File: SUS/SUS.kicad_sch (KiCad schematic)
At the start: 64 parts, among them J1 ESP32_Connector_0, J2 ESP32_Connector_1, J3 I2C, J4 I2C, J5 I2C, J6 ADC, J7 WS, U1 TJA1051T, U2 ADS8320EB_250, U3 ICM-42688-P, U4 S1001-46R, U5 S1001-46R, U6 S1001-46R

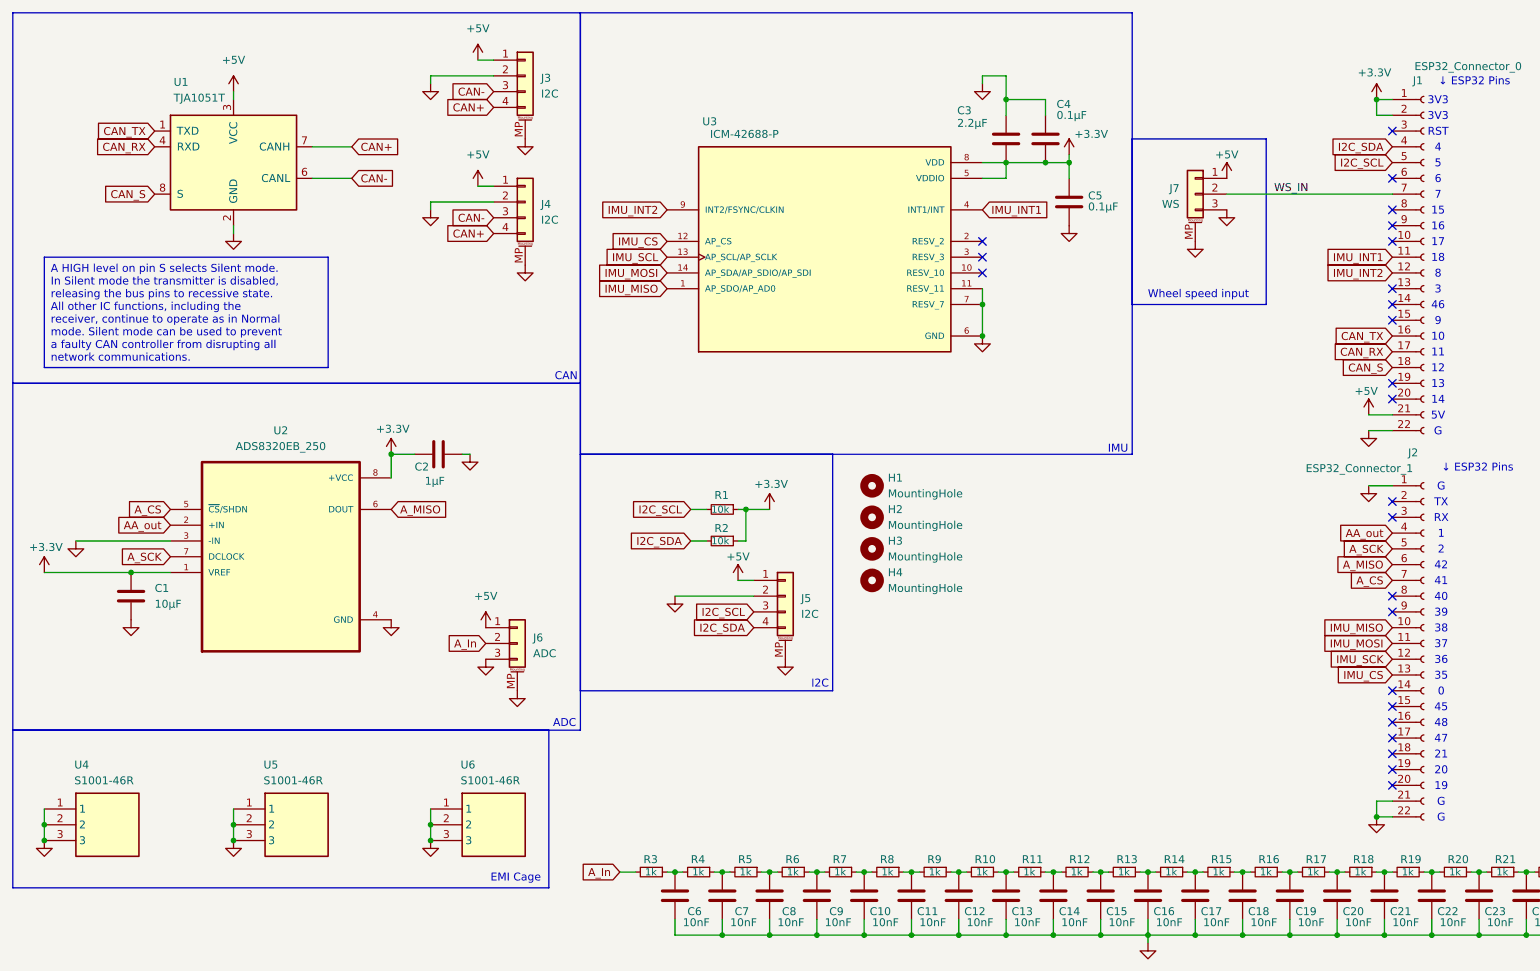
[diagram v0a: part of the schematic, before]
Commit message: added pads to connect 3.3v or 5v to lin pots & other last minute changes
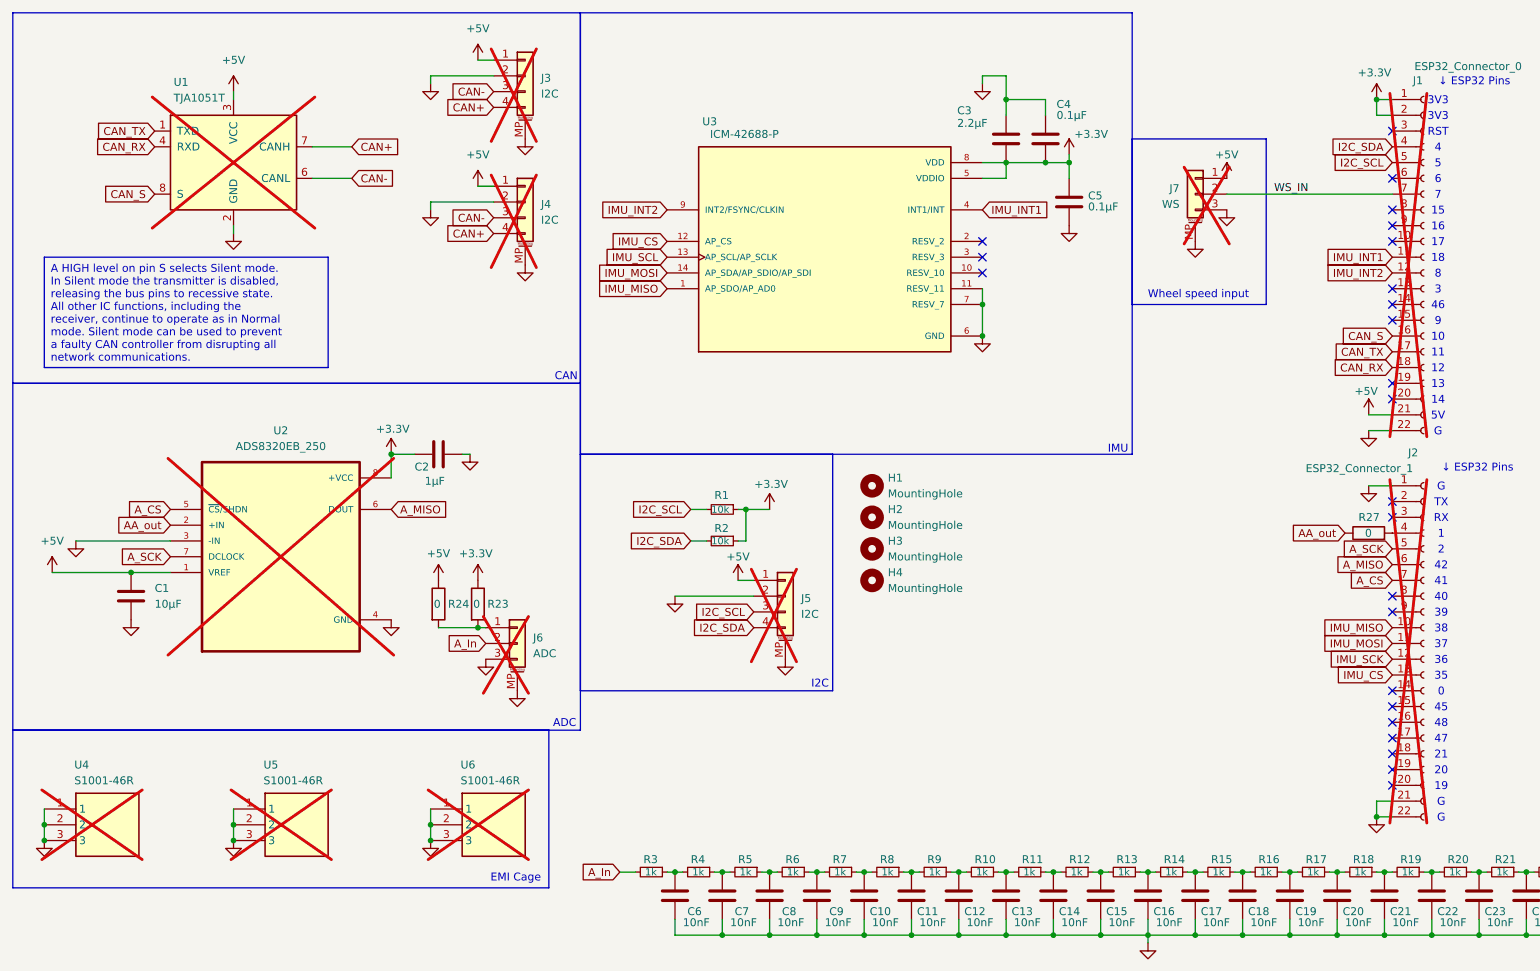
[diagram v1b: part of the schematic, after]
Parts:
- added R23, R24, R27: 0, Resistor_SMD:R_0402_1005Metric_Pad0.72x0.64mm_HandSolder, symbol Device:R
- J1, J2, J3, J4, J5, J6, J7, U1, U2, U4, U5, U6: now not fitted
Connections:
- net +3.3V: now also R23.1; no longer C1.1, U2.1 (VREF)
- net +5V: now also C1.1, U2.1 (VREF), R24.1; no longer J6.1 (Pin_1)
- net AA_out: now also R27.1; no longer J2.4 (Pin_4)
- net CAN_RX: now also J1.18 (Pin_18); no longer J1.17 (Pin_17)
- net CAN_S: now also J1.16 (Pin_16); no longer J1.18 (Pin_18)
- net CAN_TX: now also J1.17 (Pin_17); no longer J1.16 (Pin_16)
- new net: J6.1 (Pin_1), R23.2, R24.2
- new net: J2.4 (Pin_4), R27.2

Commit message: Removed Vias
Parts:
- U3: footprint ICM-42688-P:PQFN50P300X250X97-14N -> IMU:ICM-42688-P
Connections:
- net IMU_SCL is gone; now on net IMU_SCK: U3.13 (AP_SCL/AP_SCLK)
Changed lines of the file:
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@@
 		)
 	)
-	(global_label "IMU_SCL"
+	(global_label "IMU_SCK"
 		(shape input)
 		(at 118.11 52.07 180)
@@
 		)
 		(property "Intersheetrefs" "${INTERSHEET_REFS}"
-			(at 107.2629 52.07 0)
+			(at 107.021 52.07 0)
 			(effects
 				(font
@@
 			)
 		)
-		(property "Footprint" "ICM-42688-P:PQFN50P300X250X97-14N"
+		(property "Footprint" "IMU:ICM-42688-P"
 			(at 143.51 49.53 0)
 			(effects

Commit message: Complete re-design. Readme still needs to be updated.
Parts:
- removed H1, H2, H3, H4: MountingHole, MountingHole:MountingHole_2.7mm_M2.5, symbol Mechanical:MountingHole
- removed J3, J4, J5: I2C, Connector_Hirose:Hirose_DF3EA-04P-2H_1x04-1MP_P2.00mm_Horizontal, symbol Connector_Generic_MountingPin:Conn_01x04_MountingPin
- removed J6: ADC, Connector_Hirose:Hirose_DF3EA-03P-2H_1x03-1MP_P2.00mm_Horizontal, symbol Connector_Generic_MountingPin:Conn_01x03_MountingPin
- removed J7: WS, Connector_Hirose:Hirose_DF3EA-03P-2H_1x03-1MP_P2.00mm_Horizontal, symbol Connector_Generic_MountingPin:Conn_01x03_MountingPin
- removed R23, R24, R27: 0, Resistor_SMD:R_0402_1005Metric_Pad0.72x0.64mm_HandSolder, symbol Device:R
- removed U1: TJA1051T, Package_SO:SOIC-8_3.9x4.9mm_P1.27mm, symbol Interface_CAN_LIN:TJA1051T
- removed U2: ADS8320EB_250, ADS8320EB_250:DGK0008A_L, symbol ADS8320EB:ADS8320EB_250
- removed U3: ICM-42688-P, IMU:ICM-42688-P, symbol ICM-42688-P:ICM-42688-P
- removed U4, U5, U6: S1001-46R, S1001-46R:S100146R, symbol S1001-46R:S1001-46R
- added C26: 0.33μF, Capacitor_SMD:C_0603_1608Metric, symbol Device:C
- added C27: 0.1μF, Capacitor_SMD:C_0603_1608Metric, symbol Device:C
- added C28: 0.1μF, Capacitor_SMD:C_0402_1005Metric_Pad0.74x0.62mm_HandSolder, symbol Device:C
- added H1, H2, H3, H4: MountingHole_Pad, MountingHole:MountingHole_2.2mm_M2_Pad_TopOnly, symbol Mechanical:MountingHole_Pad
- added J3: D25P13A4GV00LF, D25:CONN_D25P_AMP, symbol D25:D25P13A4GV00LF
- added JP1: SolderJumper_2_Open, Jumper:SolderJumper-2_P1.3mm_Open_TrianglePad1.0x1.5mm, symbol Jumper:SolderJumper_2_Open
- added R23, R24, R25: 10k, Capacitor_SMD:C_0201_0603Metric, symbol Device:R_Small
- added U1: L7805, Package_TO_SOT_THT:TO-220F-3_Vertical, symbol Regulator_Linear:L7805
- added U2: ADS1015IDGSR, ADC:SOP50P490X110-10N, symbol ADC:ADS1015IDGSR
- added U3: ICM-42688-P, IMU:PQFN50P300X250X97-14N, symbol IMU:ICM-42688-P
- added U4: TJA1051TK-3, Package_DFN_QFN:DFN-8-1EP_3x3mm_P0.65mm_EP1.55x2.4mm, symbol Interface_CAN_LIN:TJA1051TK-3
- C1: value 10μF -> 0.1μF; footprint Capacitor_SMD:C_0402_1005Metric_Pad0.74x0.62mm_HandSolder -> Capacitor_SMD:C_0201_0603Metric
- C10, C11, C12, C13, C14, C15, C16, C17, C18, C19, C20, C21, C22, C23, C24, C25, C6, C7, C8, C9: LCSC PN C76941 -> (none)
- C2: value 1μF -> 0.1μF
- J1, J2: now fitted
- R10, R11, R12, R13, R14, R15, R16, R17, R18, R19, R20, R21, R22, R3, R4, R5, R6, R7, R8, R9: JLCpart# (none) -> C2906988; LCSC PN C270365 -> (none)
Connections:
- net WS_IN is gone; now on net CAN_RX: J1.7 (Pin_7)
- net +3.3V: now also C28.1, U3.5 (VDDIO), U3.8 (VDD), U4.5 (VIO); no longer C2.1
- net +5V: now also C2.1, C27.2, J3.16, J3.20, J3.9, U1.3 (OUT), U4.3 (VCC); no longer C1.1
- net AA_out: now also JP1.1 (A), U2.4 (AIN0)
- net A_CS: now also J2.9 (Pin_9), R25.2, U2.2 (ALERT/RDY); no longer J2.7 (Pin_7)
- net A_In: now also J3.15
- net CAN+: now also J3.10, J3.22, U4.7 (CANH)
- net CAN-: now also J3.11, J3.23, U4.6 (CANL)
- net CAN_RX: now also U4.4 (RXD); no longer J1.18 (Pin_18)
- net CAN_S: now also U4.8 (S); no longer J1.16 (Pin_16)
- net CAN_TX: now also J1.6 (Pin_6), U4.1 (TXD); no longer J1.17 (Pin_17)
- net GND: now also C26.1, C27.1, C28.2, H1.1, H2.1, H3.1, H4.1, J3.14, J3.17, J3.4, U1.2 (GND), U2.1 (ADDR), U2.3 (GND), U2.5 (AIN1), U3.11 (RESV_11), U3.6 (GND), U3.7 (RESV_7), U4.2 (GND), U4.9 (GND)
- net I2C_SCL: now also J1.4 (Pin_4), J3.19; no longer J1.5 (Pin_5)
- net I2C_SDA: now also J1.5 (Pin_5), J3.18; no longer J1.4 (Pin_4)
- net IMU_CS: now also J1.16 (Pin_16), U3.12 (AP_CS); no longer J2.13 (Pin_13)
- net IMU_INT1: now also U3.4 (INT1/INT)
- net IMU_INT2: now also U3.9 (INT2/FSYNC/CLKIN)
- net IMU_MISO: now also J1.19 (Pin_19), U3.1 (AP_SDO/AP_AD0); no longer J2.10 (Pin_10)
- net IMU_MOSI: now also J1.17 (Pin_17), U3.14 (AP_SDA/AP_SDIO/AP_SDI); no longer J2.11 (Pin_11)
- net ESP_ADC: now reaches J1.20 (Pin_20)
- net ESP_ADC: now also JP1.2 (B)
- net GPIO 20: now reaches J2.19 (Pin_19)
- net GPIO 20: now also J3.2
- net TX: now reaches J2.2 (Pin_2)
- net TX: now also J3.13
- net GPIO 19: now reaches J2.20 (Pin_20)
- net GPIO 19: now also J3.3
- net RX: now reaches J2.3 (Pin_3)
- net RX: now also J3.12
- net A_SDA: now reaches J2.8 (Pin_8)
- net A_SDA: now also R24.2, U2.9 (SDA)
- net A_MISO: no longer names the net of J2.6 (Pin_6)
- net A_SCK: no longer names the net of J2.5 (Pin_5)
- net IMU_SCK renamed GPIO 36
- net GPIO 36: now also J3.6
- new net +12V: C26.2, J3.1, U1.1 (IN)
- new net 3.3V: R23.1, R24.1, R25.1
- new net 5V: C1.1, U2.8 (VDD)
- new net A_SCL: J2.7 (Pin_7), R23.2, U2.10 (SCL)
- new net GPIO 35: J2.13 (Pin_13), J3.5
- new net GPIO 37: J2.11 (Pin_11), J3.7
- new net GPIO 38: J2.10 (Pin_10), J3.8
- new net IMU_SCL: J1.18 (Pin_18), U3.13 (AP_SCL/AP_SCLK)
- no-connect marks 24 -> 20
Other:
- note added: "3.3v pullup or 5v????"
- note removed: "EMI Cage"
- note removed: "Wheel speed input"
- moved on the sheet: R1, R2

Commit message: Changed CAN transceiver.
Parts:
- removed C28: 0.1μF, Capacitor_SMD:C_0402_1005Metric_Pad0.74x0.62mm_HandSolder, symbol Device:C
- removed H4: MountingHole_Pad, MountingHole:MountingHole_2.2mm_M2_Pad_TopOnly, symbol Mechanical:MountingHole_Pad
- removed U1: L7805, Package_TO_SOT_THT:TO-220F-3_Vertical, symbol Regulator_Linear:L7805
- removed U4: TJA1051TK-3, Package_DFN_QFN:DFN-8-1EP_3x3mm_P0.65mm_EP1.55x2.4mm, symbol Interface_CAN_LIN:TJA1051TK-3
- added U1: HT7333, HT7333:IC_HT7333, symbol HT7333:HT7333
- added U5: SN65HVD232, Package_SO:SOIC-8_3.9x4.9mm_P1.27mm, symbol Interface_CAN_LIN:SN65HVD232
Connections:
- net 3.3V is gone; now on net +3.3V: R23.1, R24.1, R25.1
- net +12V: now also U1.2 (VIN)
- net +3.3V: now also C2.1, U5.3 (VCC)
- net +5V: now also U1.3 (VOUT); no longer C2.1
- net CAN+: now also J3.11, J3.23, U5.7 (CANH); no longer J3.10, J3.22
- net CAN-: now also J3.10, J3.22, U5.6 (CANL); no longer J3.11, J3.23
- net CAN_RX: now also J2.6 (Pin_6), U5.4 (R); no longer J1.7 (Pin_7)
- net CAN_TX: now also J2.5 (Pin_5), U5.1 (D); no longer J1.6 (Pin_6)
- net GND: now also U1.1 (GND), U5.2 (GND); no longer U2.5 (AIN1)
- net I2C_SCL: now also J2.16 (Pin_16); no longer J1.4 (Pin_4)
- net I2C_SDA: now also J2.17 (Pin_17); no longer J1.5 (Pin_5)
- no-connect marks 20 -> 17

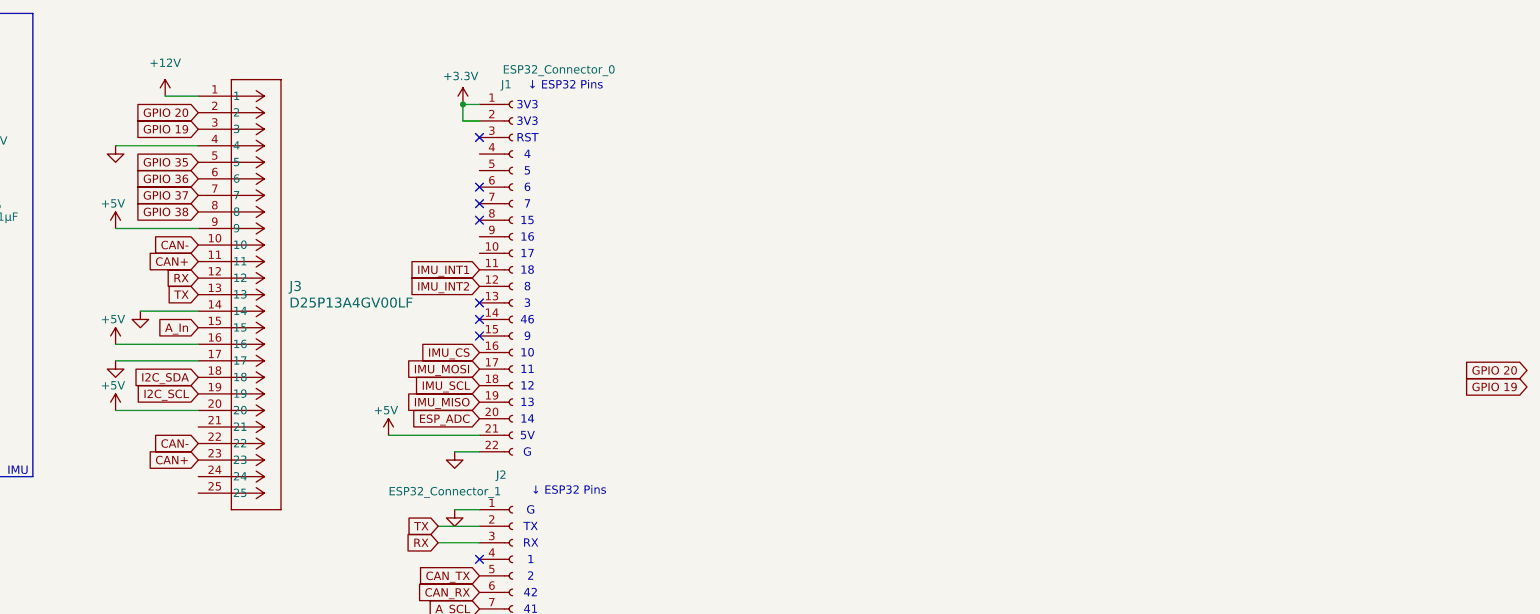
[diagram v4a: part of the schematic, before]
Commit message: Fixed DRC errors
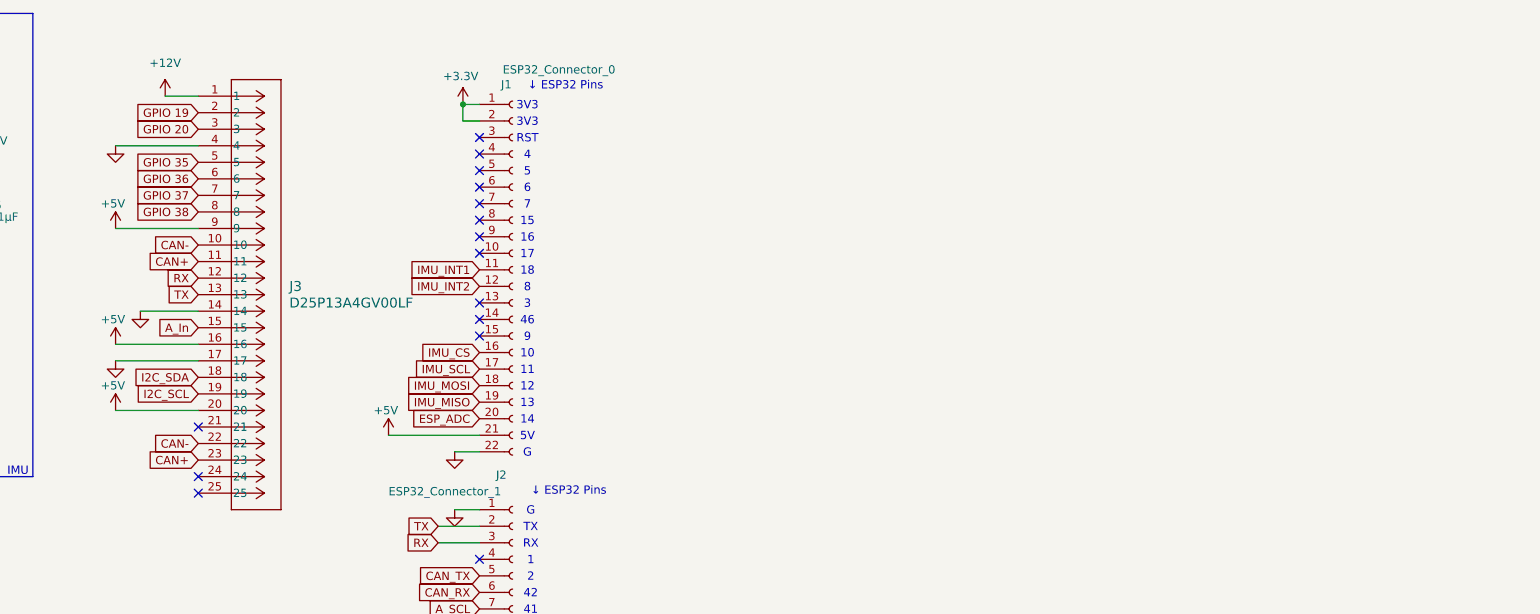
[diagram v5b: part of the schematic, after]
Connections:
- net GPIO 19: now also J3.2; no longer J3.3
- net GPIO 20: now also J3.3; no longer J3.2
- net IMU_MOSI: now also J1.18 (Pin_18); no longer J1.17 (Pin_17)
- net IMU_SCL: now also J1.17 (Pin_17); no longer J1.18 (Pin_18)
- no-connect marks 17 -> 24

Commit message: Minor Changes
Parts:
- U1: value HT7333 -> HT7350-A
- renumbered U5 to U4
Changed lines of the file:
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@@
 		(dnp no)
 		(fields_autoplaced yes)
-		(property "Reference" "U5"
+		(property "Reference" "U4"
 			(at 60.6141 25.4 0)
 			(effects
@@
 			(project ""
 				(path "/4bc4e24b-850f-49e9-945b-9f19aae95ccf"
-					(reference "U5")
+					(reference "U4")
 					(unit 1)
 				)
@@
 			)
 		)
-		(property "Value" "HT7333"
+		(property "Value" "HT7350-A"
 			(at 52.07 123.19 0)
 			(effects

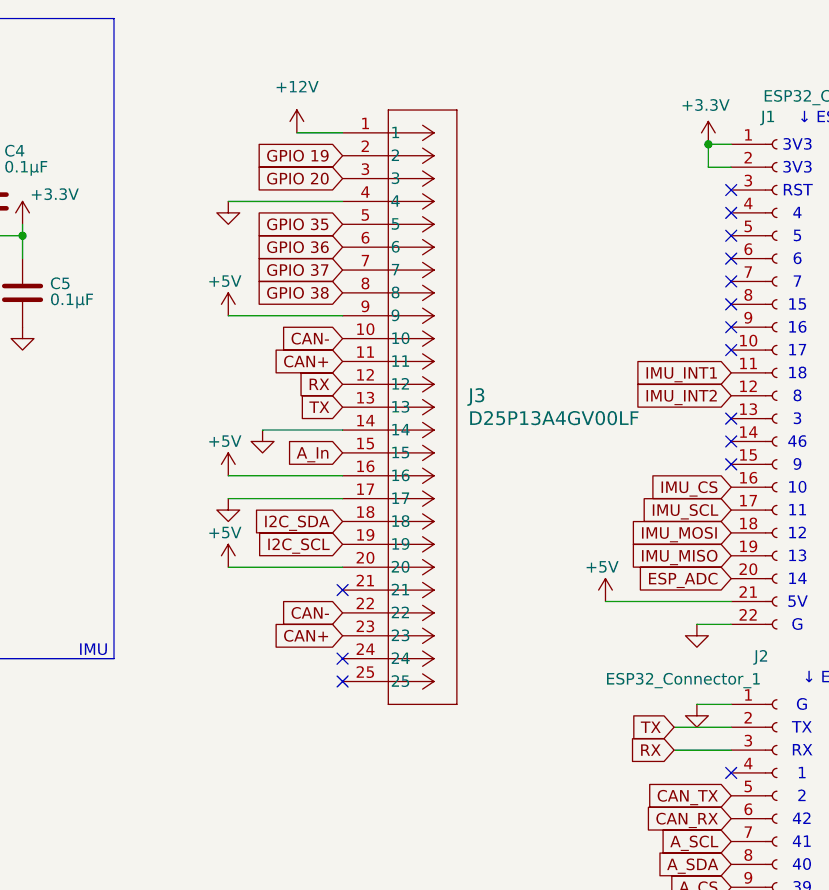
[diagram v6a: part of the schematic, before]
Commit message: Added jumpers for 5v and 3v3 for lin pot
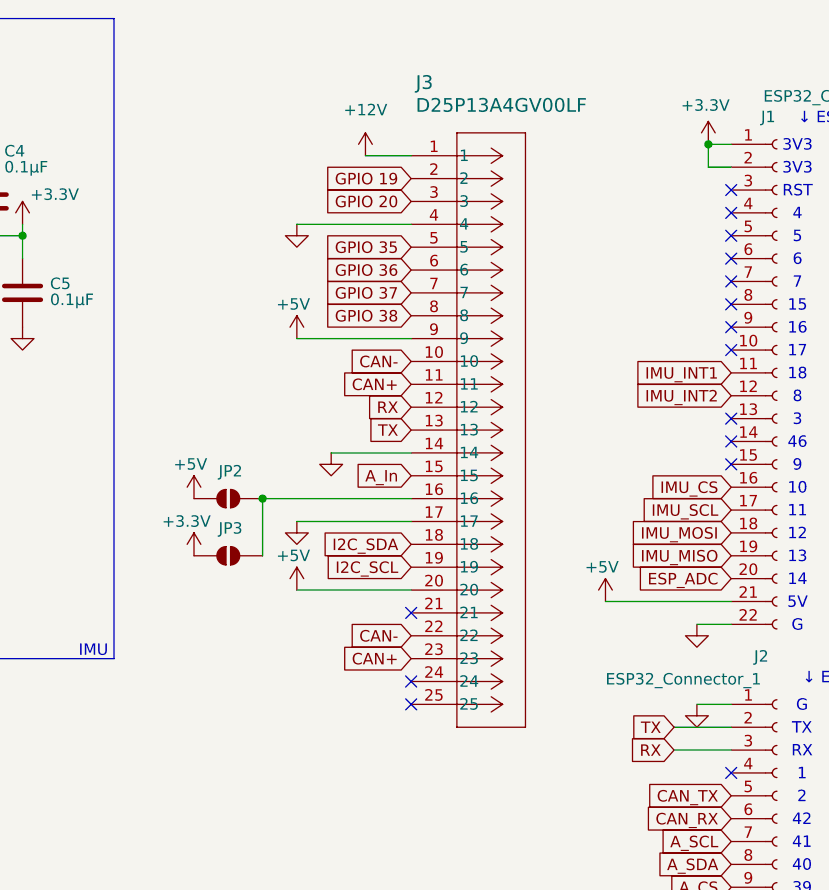
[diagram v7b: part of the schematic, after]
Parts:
- added JP2, JP3: SolderJumper_2_Open, Jumper:SolderJumper-2_P1.3mm_Open_TrianglePad1.0x1.5mm, symbol Jumper:SolderJumper_2_Open
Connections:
- net +3.3V: now also JP3.1 (A)
- net +5V: now also JP2.1 (A); no longer J3.16
- new net: J3.16, JP2.2 (B), JP3.2 (B)
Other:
- moved on the sheet: J3
